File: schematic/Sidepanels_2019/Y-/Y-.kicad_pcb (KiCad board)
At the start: 2 copper layers, 327.5 x 83 mm, 53 parts, among them J1 Conn_01x04, J2 Conn_01x02

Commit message: Flipped and/or added TrisolX cells
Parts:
- added D26: D_Schottky, CySat footprints:Toshiba_CUS08F30, B.Cu at (13.2, 62.1)
- added D27: D_Schottky, CySat footprints:Toshiba_CUS08F30, B.Cu at (13.1, 110.3)
- added D28: D_Schottky, CySat footprints:Toshiba_CUS08F30, B.Cu at (16.3, 62.1)
- added D29: D_Schottky, CySat footprints:Toshiba_CUS08F30, B.Cu at (16.3, 110.3)
- added D30: D_Schottky, CySat footprints:Toshiba_CUS08F30, B.Cu at (22.6, 110.3)
- added D31: D_Schottky, CySat footprints:Toshiba_CUS08F30, B.Cu at (32.1, 62.1)
- added D32: D_Schottky, CySat footprints:Toshiba_CUS08F30, B.Cu at (19.5, 110.3)
- added D33: D_Schottky, CySat footprints:Toshiba_CUS08F30, B.Cu at (32.1, 110.3)
- added D34: D_Schottky, CySat footprints:Toshiba_CUS08F30, B.Cu at (28.9, 62.1)
- added D35: D_Schottky, CySat footprints:Toshiba_CUS08F30, B.Cu at (28.9, 110.3)
- added D36: D_Schottky, CySat footprints:Toshiba_CUS08F30, B.Cu at (22.7, 62.1)
- added D37: D_Schottky, CySat footprints:Toshiba_CUS08F30, B.Cu at (19.5, 62.1)
- added D38: D_Schottky, CySat footprints:Toshiba_CUS08F30, B.Cu at (25.8, 62.1)
- added D39: D_Schottky, CySat footprints:Toshiba_CUS08F30, B.Cu at (25.8, 110.3)
- added SC27: Solar_Cell, CySat footprints:TriSelectSolarPanel_Left_Handed, F.Cu at (294.9, 80.9)
- added SC28: Solar_Cell, CySat footprints:TriSelectSolarPanel_Left_Handed, F.Cu at (294.9, 71.6)
- added SC29: Solar_Cell, CySat footprints:TriSelectSolarPanel_Left_Handed, F.Cu at (295.0, 53.5)
- added SC30: Solar_Cell, CySat footprints:TriSelectSolarPanel_Left_Handed, F.Cu at (294.9, 62.2)
- added SC31: Solar_Cell, CySat footprints:TriSelectSolarPanel_Left_Handed, F.Cu at (141.1, 119.8)
- added SC32: Solar_Cell, CySat footprints:TriSelectSolarPanel_Left_Handed, F.Cu at (106.0, 128.5)
- added SC33: Solar_Cell, CySat footprints:TriSelectSolarPanel_Left_Handed, F.Cu at (166.6, 128.7)
- added SC34: Solar_Cell, CySat footprints:TriSelectSolarPanel_Left_Handed, F.Cu at (63.4, 87.9)
- added SC35: Solar_Cell, CySat footprints:TriSelectSolarPanel_Left_Handed, F.Cu at (137.1, 70.8)
- added SC36: Solar_Cell, CySat footprints:TriSelectSolarPanel_Left_Handed, F.Cu at (63.4, 79.2)
- added SC37: Solar_Cell, CySat footprints:TriSelectSolarPanel_Left_Handed, F.Cu at (63.3, 96.5)
- added SC38: Solar_Cell, CySat footprints:TriSelectSolarPanel_Left_Handed, F.Cu at (63.3, 105.0)
- added SC39: Solar_Cell, CySat footprints:TriSelectSolarPanel_Left_Handed, F.Cu at (63.4, 122.3)
- added SC40: Solar_Cell, CySat footprints:TriSelectSolarPanel_Left_Handed, F.Cu at (63.3, 113.7)
- SC10, SC11, SC12, SC13, SC14, SC15, SC16, SC17, SC2, SC20, SC21, SC22, SC23, SC24, SC25, SC26, SC3, SC4, SC5, SC6, SC7, SC8, SC9: footprint CySat footprints:TriSelectSolarPanel -> CySat footprints:TriSelectSolarPanel_Left_Handed
- moved SC4 69.9 mm to (30.6, 122.3), turned to 0 degrees
- moved SC11 67.6 mm to (4.09, 54.1), turned to 180 degrees
- moved SC6 57.8 mm to (63.4, 62.0), turned to 0 degrees
- moved SC25 56.2 mm to (30.6, 62.3), turned to 0 degrees
- moved SC12 54.9 mm to (4.09, 114.1), turned to 180 degrees
- moved SC5 53.6 mm to (30.7, 113.7), turned to 0 degrees
- moved SC15 50.8 mm to (4.09, 62.7), turned to 180 degrees
- moved SC20 42.5 mm to (294.9, 98.3), turned to 180 degrees
- moved SC23 40.5 mm to (30.6, 70.8), turned to 0 degrees
- moved SC26 38.4 mm to (4.09, 105.5), turned to 180 degrees
- moved SC7 38.1 mm to (30.6, 105.1), turned to 0 degrees
- moved SC14 35.0 mm to (294.9, 89.7), turned to 180 degrees
- moved SC17 34.5 mm to (4.09, 71.2), turned to 180 degrees
- moved SC16 26.7 mm to (30.6, 79.4), turned to 0 degrees
- moved SC9 24.9 mm to (30.6, 96.5), turned to 0 degrees
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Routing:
- net VCC: track 59.1 -> 135.0 mm, vias 26 -> 40
- net VSS: track 276.3 -> 336.1 mm, vias 33 -> 47

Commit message: Fixed TrisolX Cells
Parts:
- removed D35, D36, D37, D38, D39: D_Schottky, CySat footprints:Toshiba_CUS08F30
- removed SC36, SC37, SC38, SC39, SC40: Solar_Cell, CySat footprints:TriSelectSolarPanel_Left_Handed
- moved SC3 30.8 mm to (62.8, 101.4), turned to 90 degrees
- moved SC34 18.4 mm to (75.9, 101.4), turned to 90 degrees
- moved SC6 8.94 mm to (69.0, 68.9), turned to 90 degrees
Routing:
- net VSS: track 336.1 -> 319.3 mm, vias 47 -> 42
- net VCC: track 135.0 -> 119.4 mm, vias 40 -> 35

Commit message: Completed y-
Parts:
- removed D10, D11, D12, D13, D14, D15, D16, D17, D18, D19, D2, D20, D21, D22, D23, D24, D26, D27, D28, D29, D3, D30, D31, D32, D33, D34, D4, D5, D6, D7, D8, D9: D_Schottky, CySat footprints:Toshiba_CUS08F30
- removed D25: D_Photo, CySat footprints:Sun_Sensor
- removed SC10, SC11, SC12, SC13, SC14, SC15, SC16, SC17, SC20, SC21, SC22, SC23, SC24, SC25, SC26, SC27, SC28, SC29, SC30, SC31, SC32, SC33, SC34, SC35, SC7, SC8, SC9: Solar_Cell, CySat footprints:TriSelectSolarPanel_Left_Handed
- removed SC18, SC19: Solar_Cell, CySat footprints:Spectrolab
- D1: value D_Schottky -> D_Photo; footprint CySat footprints:Toshiba_CUS08F30 -> Diode_SMD:D_0805_2012Metric; moved to F.Cu
- SC1: footprint CySat footprints:ISS_SolarCell -> CySat_Solar:Spectrolab
- SC2, SC3, SC4, SC5, SC6: footprint CySat footprints:TriSelectSolarPanel_Left_Handed -> CySat_Solar:Spectrolab
- moved D1 318.3 mm to (313.7, 208.9), turned to 270 degrees
- moved SC6 295.4 mm to (334.6, 198.1), turned to 270 degrees
- moved SC3 203.6 mm to (241.9, 198.1), turned to 270 degrees
- moved SC1 197.1 mm to (380.4, 198.1), turned to 270 degrees
- moved J1 192.9 mm to (183.8, 201.0)
- moved J2 192.9 mm to (183.8, 187.2)
- moved SC4 182.8 mm to (196.8, 198.1), turned to 270 degrees
- moved SC2 159.0 mm to (425.4, 198.1), turned to 270 degrees
- moved SC5 147.6 mm to (151.8, 198.1), turned to 270 degrees
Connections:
- D1 pad 1: VCC -> Net-(D1-Pad1)
- D1 pad 2: VSS -> Net-(D1-Pad2)
- J2 pad 1: Net-(D25-Pad2) -> Net-(D1-Pad2)
- J2 pad 2: Net-(D25-Pad1) -> Net-(D1-Pad1)
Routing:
- net VSS: track 319.3 -> 40.0 mm, vias 42 -> 6
- net Net-(D1-Pad2): track 0.00 -> 137.7 mm, vias 0 -> 1
- net Net-(D1-Pad1): track 0.00 -> 137.5 mm, vias 0 -> 1
- net Net-(D25-Pad2): track 130.6 -> 0.00 mm, vias 1 -> 0
- net Net-(D25-Pad1): track 121.7 -> 0.00 mm, vias 1 -> 0
- net VCC: track 119.4 -> 27.6 mm, vias 35 -> 1
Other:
- outline, holes or cut-outs redrawn

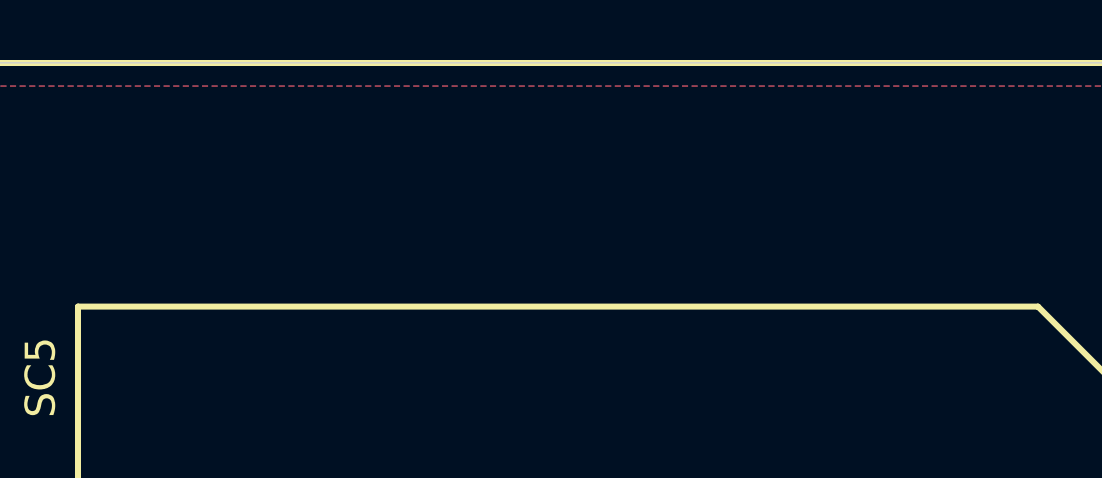
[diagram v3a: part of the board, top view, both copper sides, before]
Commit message: Update to all boards
Added labels to boards to resolve issue #2
Added names of students and faculty to boards
Generated Step files to resolve issue #4, please note the export does include the silkscreen.
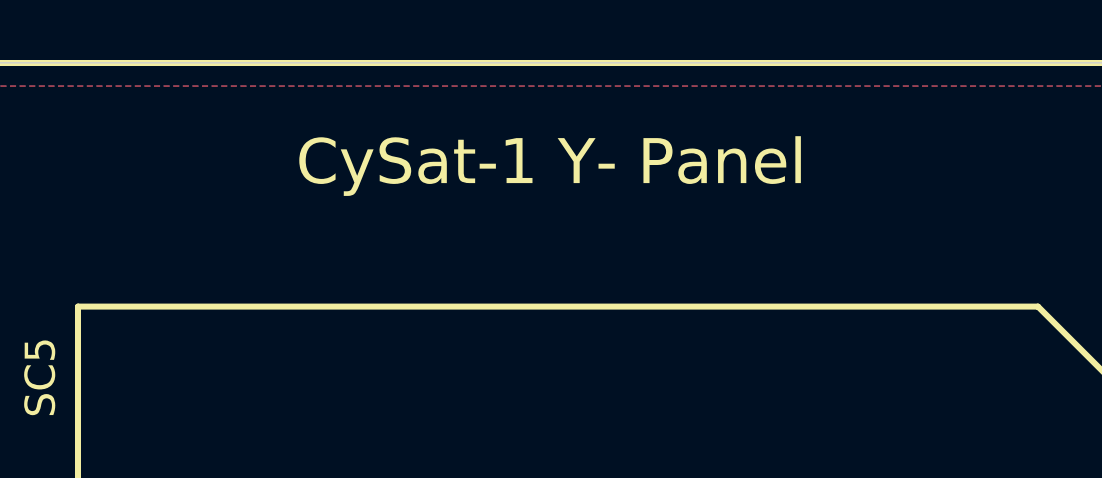
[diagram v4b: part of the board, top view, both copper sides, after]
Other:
- board text added: "CySat-1 Y- Panel"

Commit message: Push of all changes made for June update
Major change was in the solar cell and creating a new library based on the old one.
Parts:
- SC1, SC2, SC3, SC4, SC5, SC6: footprint CySat_Solar:Spectrolab -> CySat:Spectrolabs_UTJ
- moved J2 142.9 mm to (325.1, 208.4), turned to -90 degrees
- moved SC2 24.5 mm to (450.0, 199.2)
- moved SC3 24.0 mm to (265.8, 200.3)
- moved SC5 23.6 mm to (175.4, 197.5)
- moved SC1 23.4 mm to (403.7, 199.3)
- moved SC4 23.3 mm to (220.1, 198.2)
- moved SC6 22.0 mm to (356.6, 199.1)
- moved D1 0.82 mm to (313.7, 208.1), turned to 90 degrees
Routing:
- net Net-(D1-Pad2): track 137.7 -> 10.5 mm
- net Net-(D1-Pad1): track 137.5 -> 10.3 mm
- net VSS: track 40.0 -> 104.5 mm, vias 6 -> 12
- net VCC: track 27.6 -> 7.63 mm
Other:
- net class Default removed
- rule pad_to_mask_clearance: 0.051 -> 0
